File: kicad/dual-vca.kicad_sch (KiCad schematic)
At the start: 57 parts, among them J1 Eurorack Mono Jack, J2 Eurorack Mono Jack, J3 Eurorack Mono Jack, J4 Eurorack Mono Jack, J5 Eurorack Power Small, J6 Eurorack Mono Jack, J7 Eurorack Mono Jack, J8 Conn_02x06_Odd_Even, J9 Conn_02x06_Odd_Even, U1 SSI2164, U2 TL074, U3 LM4040LP-10, U4 LM4040LP-2.5

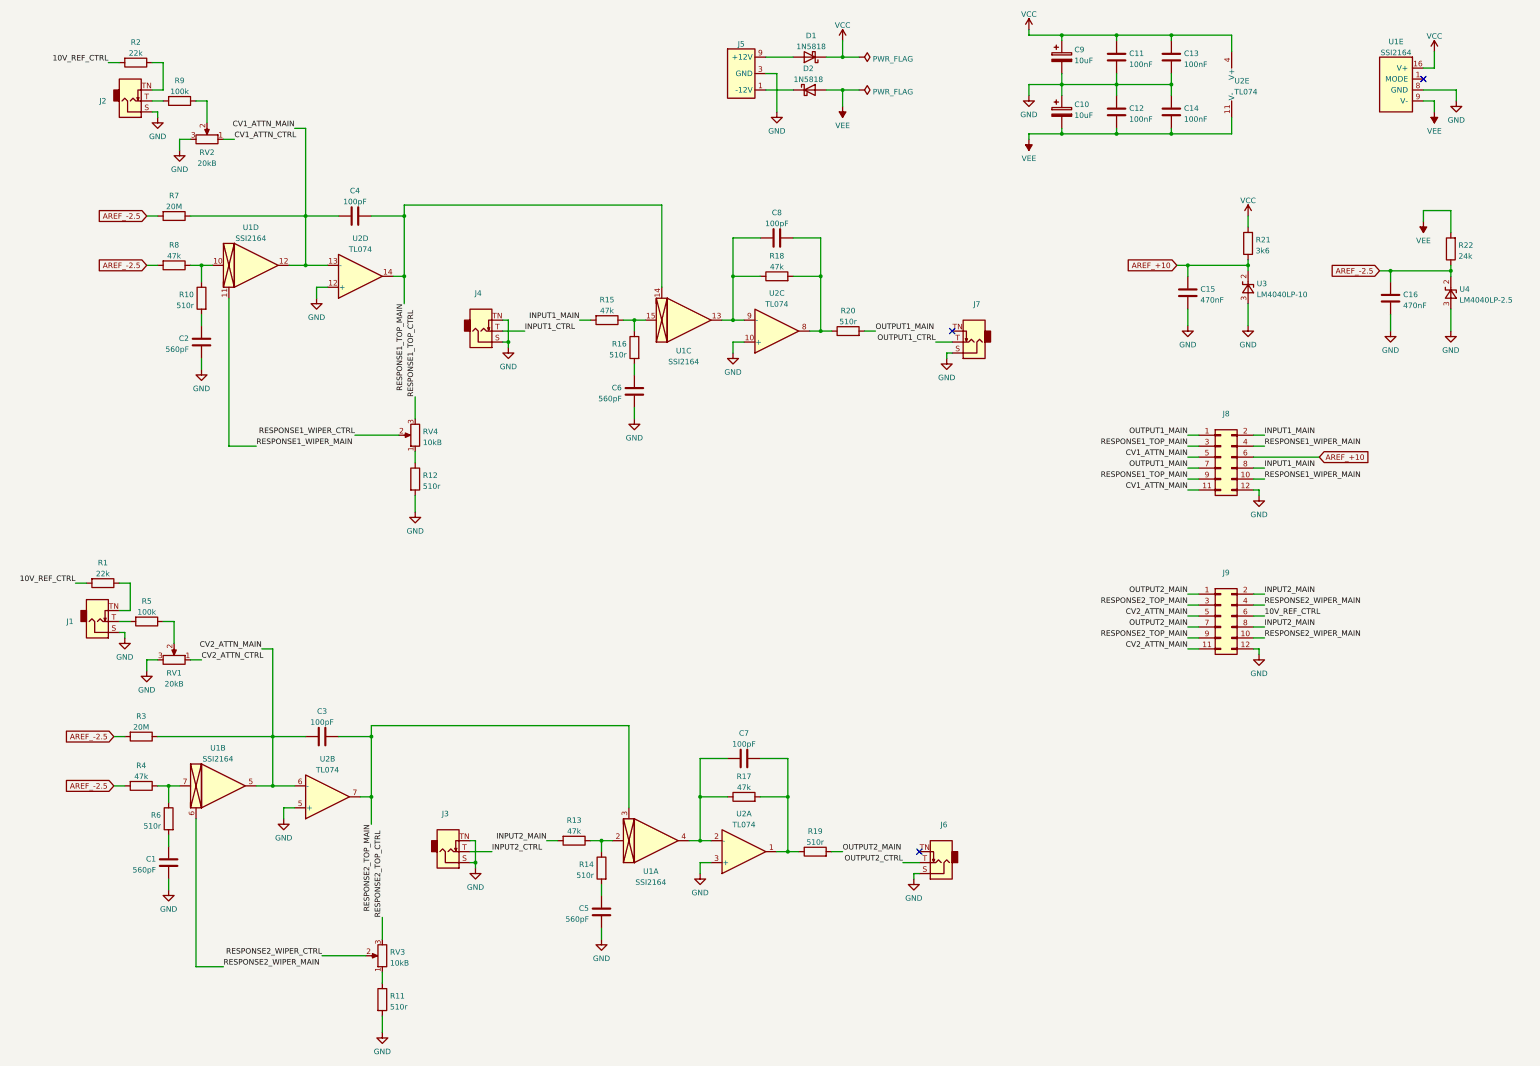
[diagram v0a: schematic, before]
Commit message: Adding beginnings of panel files and routed more of the pcb
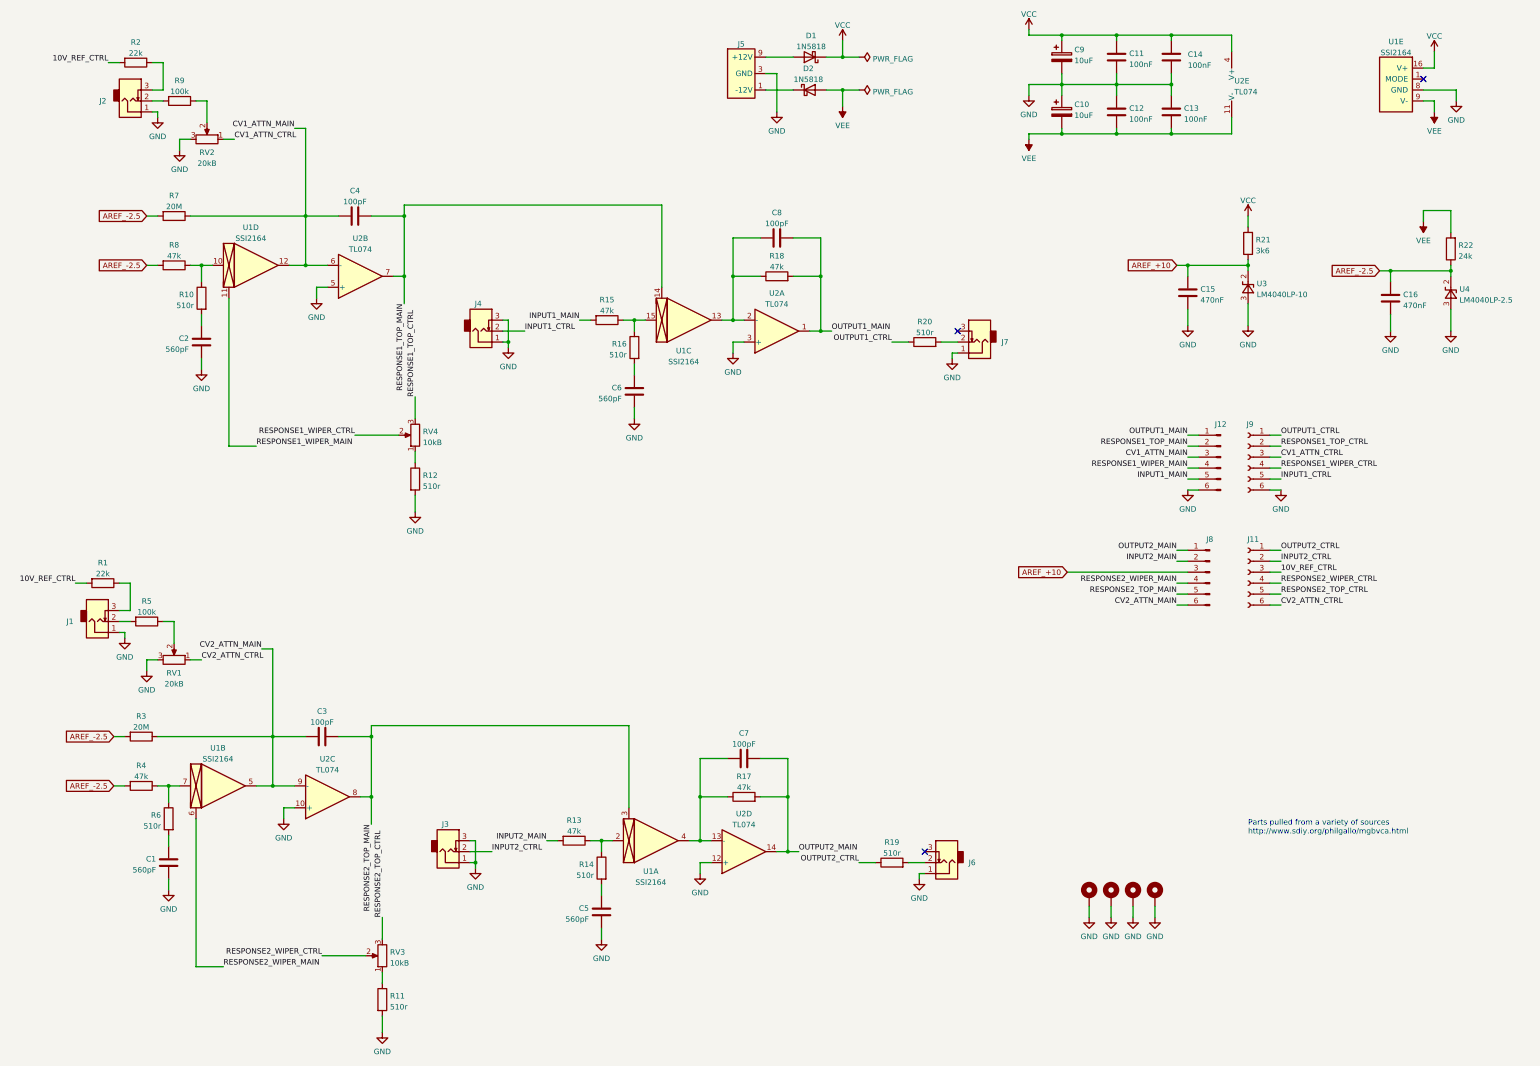
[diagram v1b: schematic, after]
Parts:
- removed J8: Conn_02x06_Odd_Even, Connector_PinHeader_2.54mm:PinHeader_2x06_P2.54mm_Vertical, symbol Connector_Generic:Conn_02x06_Odd_Even
- removed J9: Conn_02x06_Odd_Even, Connector_PinSocket_2.54mm:PinSocket_2x06_P2.54mm_Vertical, symbol Connector_Generic:Conn_02x06_Odd_Even
- added H1, H2, H3, H4: MountingHole_Pad, MountingHole:MountingHole_3.2mm_M3_DIN965_Pad, symbol Mechanical:MountingHole_Pad
- added J11, J9: Conn_01x06_Socket, Connector_PinSocket_2.54mm:PinSocket_1x06_P2.54mm_Vertical, symbol Connector:Conn_01x06_Socket
- added J12, J8: Conn_01x06_Pin, Connector_PinHeader_2.54mm:PinHeader_1x06_P2.54mm_Vertical, symbol Connector:Conn_01x06_Pin
- C1, C11, C12, C13, C14, C15, C16, C2, C3, C4, C5, C6, C7, C8: footprint rumblesan-standard-parts:C_Rect_L7.0mm_W3.5mm_P5.00mm -> Rumblesan_Standard_Parts:C_Rect_L7.0mm_W2.5mm_P5.00mm
- C10, C9: footprint rumblesan-standard-parts:CP_Radial_D5.0mm_P2.00mm -> Rumblesan_Standard_Parts:CP_Radial_D5.0mm_P2.00mm
- D1, D2: footprint rumblesan-standard-parts:D_DO-41_SOD81_P10.16mm_Horizontal -> Rumblesan_Standard_Parts:D_DO-41_SOD81_P10.16mm_Horizontal
- J1, J2, J3, J4, J6, J7: footprint rumblesan-standard-parts:Jack_3.5mm_QingPu_WQP-PJ398SM_Vertical -> Rumblesan_Standard_Parts:Jack_3.5mm_QingPu_WQP-PJ398SM_Vertical; symbol Eurorack_Hardware:Eurorack Mono Jack -> Audio_Connectors:Eurorack_Mono_Jack
- J5: footprint eurorack-power:Eurorack_PowerHeader_2x05_P2.54mm_Shrouded -> Eurorack_Power:Eurorack_PowerHeader_2x05_P2.54mm_Shrouded
- R1, R10, R11, R12, R13, R14, R15, R16, R17, R18, R19, R2, R20, R21, R22, R3, R4, R5, R6, R7, R8, R9: footprint rumblesan-standard-parts:R_Axial_DIN0207_L6.3mm_D2.5mm_P10.16mm_Horizontal -> Rumblesan_Standard_Parts:R_Axial_DIN0207_L6.3mm_D2.5mm_P10.16mm_Horizontal
- RV1, RV2, RV3, RV4: footprint rumblesan-standard-parts:Potentiometer_Alpha_RD901F-40-00D_Single_Vertical -> Rumblesan_Standard_Parts:Potentiometer_Alpha_RD901F-40-00D_Single_Vertical
- U1: footprint rumblesan-standard-parts:DIP-16_W7.62mm_Socket -> Package_DIP:DIP-16_W7.62mm_Socket
- U2: footprint rumblesan-standard-parts:DIP-14_W7.62mm_Socket -> Package_DIP:DIP-14_W7.62mm_Socket
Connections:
- net 10V_REF_CTRL: now also J11.3 (Pin_3)
- net AREF_+10: now also J8.3 (Pin_3)
- net CV1_ATTN_CTRL: now also J9.3 (Pin_3)
- net CV1_ATTN_MAIN: now also U2.6 (-), J12.3 (Pin_3); no longer U2.13 (-)
- net CV2_ATTN_CTRL: now also J11.6 (Pin_6)
- net CV2_ATTN_MAIN: now also U2.9 (-), J8.6 (Pin_6); no longer U2.6 (-)
- net GND: now also C13.1, J1.1 (Sleeve), J2.1 (Sleeve), J3.1 (Sleeve), J3.3 (Tip_normalize), J4.1 (Sleeve), J4.3 (Tip_normalize), J6.1 (Sleeve), J7.1 (Sleeve), H1.1, H2.1, H3.1, H4.1, J12.6 (Pin_6), J9.6 (Pin_6); no longer C13.2, J1.S (Sleeve), J2.S (Sleeve), J3.S (Sleeve), J3.TN (Tip_normalize), J4.S (Sleeve), J4.TN (Tip_normalize), J6.S (Sleeve), J7.S (Sleeve)
- net INPUT1_CTRL: now also J4.2 (Tip), J9.5 (Pin_5); no longer J4.T (Tip)
- net INPUT1_MAIN: now also J12.5 (Pin_5)
- net INPUT2_CTRL: now also J3.2 (Tip), J11.2 (Pin_2); no longer J3.T (Tip)
- net INPUT2_MAIN: now also J8.2 (Pin_2)
- net OUTPUT1_CTRL: now also R20.1, J9.1 (Pin_1); no longer J7.T (Tip)
- net OUTPUT1_MAIN: now also C8.2, R18.2, U2.1, J12.1 (Pin_1); no longer R20.2
- net OUTPUT2_CTRL: now also R19.1, J11.1 (Pin_1); no longer J6.T (Tip)
- net OUTPUT2_MAIN: now also C7.2, R17.2, U2.14, J8.1 (Pin_1); no longer R19.2
- net RESPONSE1_TOP_CTRL: now also J9.2 (Pin_2)
- net RESPONSE1_TOP_MAIN: now also U2.7, J12.2 (Pin_2); no longer U2.14
- net RESPONSE1_WIPER_CTRL: now also J9.4 (Pin_4)
- net RESPONSE1_WIPER_MAIN: now also J12.4 (Pin_4)
- net RESPONSE2_TOP_CTRL: now also J11.5 (Pin_5)
- net RESPONSE2_TOP_MAIN: now also U2.8, J8.5 (Pin_5); no longer U2.7
- net RESPONSE2_WIPER_CTRL: now also J11.4 (Pin_4)
- net RESPONSE2_WIPER_MAIN: now also J8.4 (Pin_4)
- net VCC: now also C14.2; no longer C13.1
- net VEE: now also C13.2; no longer C14.2
- net at C8.1, R18.1, U1.13: now also U2.2 (-); no longer U2.9 (-)
- net at R2.1: now also J2.3 (Tip_normalize); no longer J2.TN (Tip_normalize)
- net at R5.2: now also J1.2 (Tip); no longer J1.T (Tip)
- net at R1.1: now also J1.3 (Tip_normalize); no longer J1.TN (Tip_normalize)
- net at R9.2: now also J2.2 (Tip); no longer J2.T (Tip)
- net at C7.1, R17.1, U1.4: now also U2.13 (-); no longer U2.2 (-)
- new net: J6.2 (Tip), R19.2
- new net: J7.2 (Tip), R20.2
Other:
- note added: "Parts pulled from a variety of sources http://www.sdiy.org/philgallo/mgbvca.html"
- moved on the sheet: C13, C14, J6, J7, R19, R20, U2A, U2B, U2C, U2D

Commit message: Finishing routing PCBs
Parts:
- C1, C11, C12, C13, C14, C15, C16, C2, C3, C4, C5, C6, C7, C8: footprint Rumblesan_Standard_Parts:C_Rect_L7.0mm_W2.5mm_P5.00mm -> Capacitor_THT:C_Rect_L7.0mm_W2.5mm_P5.00mm; symbol rumblesan-standard-parts:C -> Device:C
- C10, C9: footprint Rumblesan_Standard_Parts:CP_Radial_D5.0mm_P2.00mm -> Capacitor_THT:CP_Radial_D5.0mm_P2.00mm; symbol rumblesan-standard-parts:C_Polarized -> Device:C_Polarized
- D1, D2: footprint Rumblesan_Standard_Parts:D_DO-41_SOD81_P10.16mm_Horizontal -> Diode_THT:D_DO-41_SOD81_P10.16mm_Horizontal
- J5: symbol Eurorack_Hardware:Eurorack Power Small -> Eurorack_Power:Eurorack Power Small
- R1, R10, R11, R12, R13, R14, R15, R16, R17, R18, R19, R2, R20, R21, R22, R3, R4, R5, R6, R7, R8, R9: footprint Rumblesan_Standard_Parts:R_Axial_DIN0207_L6.3mm_D2.5mm_P10.16mm_Horizontal -> Resistor_THT:R_Axial_DIN0207_L6.3mm_D2.5mm_P10.16mm_Horizontal; symbol rumblesan-standard-parts:R -> Device:R
- U3, U4: footprint Package_TO_SOT_THT:TO-92_Inline -> Package_TO_SOT_THT:TO-92_Inline_Wide
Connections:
- net 10V_REF_CTRL: now also C15.1, R1.1, R2.1, R21.2, U3.2 (K); no longer J11.3 (Pin_3), R1.2, R2.2
- net AREF_-2.5: now also R22.2, R3.1, R4.1, R7.1, R8.1; no longer R22.1, R3.2, R4.2, R7.2, R8.2
- net CV1_ATTN_CTRL: now also J9.5 (Pin_5); no longer J9.3 (Pin_3)
- net CV1_ATTN_MAIN: now also J12.5 (Pin_5), R7.2; no longer J12.3 (Pin_3), R7.1
- net CV2_ATTN_CTRL: now also J11.5 (Pin_5); no longer J11.6 (Pin_6)
- net CV2_ATTN_MAIN: now also J8.5 (Pin_5), R3.2; no longer J8.6 (Pin_6), R3.1
- net GND: now also J11.3 (Pin_3), J8.3 (Pin_3), R11.1, R12.1; no longer J12.6 (Pin_6), J9.6 (Pin_6), R11.2, R12.2
- net INPUT1_CTRL: now also J9.2 (Pin_2); no longer J9.5 (Pin_5)
- net INPUT1_MAIN: now also J12.2 (Pin_2), R15.1; no longer J12.5 (Pin_5), R15.2
- net INPUT2_MAIN: now also R13.1; no longer R13.2
- net OUTPUT1_CTRL: now also R20.2; no longer R20.1
- net OUTPUT1_MAIN: now also R18.1; no longer R18.2
- net OUTPUT2_CTRL: now also R19.2; no longer R19.1
- net OUTPUT2_MAIN: now also R17.1; no longer R17.2
- net RESPONSE1_TOP_CTRL: now also J9.4 (Pin_4); no longer J9.2 (Pin_2)
- net RESPONSE1_TOP_MAIN: now also J12.4 (Pin_4); no longer J12.2 (Pin_2)
- net RESPONSE1_WIPER_CTRL: now also J9.6 (Pin_6); no longer J9.4 (Pin_4)
- net RESPONSE1_WIPER_MAIN: now also J12.6 (Pin_6); no longer J12.4 (Pin_4)
- net RESPONSE2_TOP_CTRL: now also J11.4 (Pin_4); no longer J11.5 (Pin_5)
- net RESPONSE2_TOP_MAIN: now also J8.4 (Pin_4); no longer J8.5 (Pin_5)
- net RESPONSE2_WIPER_CTRL: now also J11.6 (Pin_6); no longer J11.4 (Pin_4)
- net RESPONSE2_WIPER_MAIN: now also J8.6 (Pin_6); no longer J8.4 (Pin_4)
- net VCC: now also J12.3 (Pin_3); no longer R21.2
- net VEE: now also R22.1; no longer R22.2
- net at C8.1, U1.13, U2.2 (-): now also R18.2; no longer R18.1
- net at RV4.1: now also R12.2; no longer R12.1
- net at J2.3 (Tip_normalize): now also R2.2; no longer R2.1
- net at RV3.1: now also R11.2; no longer R11.1
- net at C7.1, U1.4, U2.13 (-): now also R17.2; no longer R17.1
- net at J6.2 (Tip): now also R19.1; no longer R19.2
- net at J1.2 (Tip): now also R5.1; no longer R5.2
- net at J1.3 (Tip_normalize): now also R1.2; no longer R1.1
- net at RV1.2: now also R5.2; no longer R5.1
- net at C5.2: now also R14.1; no longer R14.2
- net at R16.2: now also R15.2, U1.15; no longer C6.2
- net at C1.2: now also R6.1; no longer R6.2
- net at R9.1: now also J2.2 (Tip); no longer RV2.2
- net at R9.2: now also RV2.2; no longer J2.2 (Tip)
- net at R10.2: now also R8.2, U1.10; no longer C2.2
- net at J7.2 (Tip): now also R20.1; no longer R20.2
- removed net AREF_+10: C15.1, J8.3 (Pin_3), R21.1, U3.2 (K)
- new net: C6.2, R16.1
- new net: R4.2, R6.2, U1.7
- new net: R13.2, R14.2, U1.2
- new net: C2.2, R10.1
- new net VCC_CTRL: J9.3 (Pin_3), R21.1

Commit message: Fixes for revision 2
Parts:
- added R23: 6k8, Resistor_THT:R_Axial_DIN0207_L6.3mm_D2.5mm_P10.16mm_Horizontal, symbol Device:R
- H1, H2, H3, H4: now left out of the parts list
- J1, J2, J3, J4, J6, J7: footprint Rumblesan_Standard_Parts:Jack_3.5mm_QingPu_WQP-PJ398SM_Vertical -> Rumblesan_Audio_Connectors:Jack_3.5mm_QingPu_WQP-PJ398SM_Vertical; symbol Audio_Connectors:Eurorack_Mono_Jack -> Connector_Audio:AudioJack2_SwitchT
- J5: footprint Eurorack_Power:Eurorack_PowerHeader_2x05_P2.54mm_Shrouded -> Rumblesan_Eurorack_Power:Eurorack_PowerHeader_2x05_P2.54mm_Shrouded; symbol Eurorack_Power:Eurorack Power Small -> Rumblesan_Eurorack_Power:Eurorack Power Small
- R21: value 3k6 -> 1k
- R22: value 24k -> 47k
- RV1, RV2, RV3, RV4: footprint Rumblesan_Standard_Parts:Potentiometer_Alpha_RD901F-40-00D_Single_Vertical -> Rumblesan_Potentiometer_THT:Potentiometer_Alpha_RD901F-40-00D_Single_Vertical
- U1: symbol Audio_Chips:SSI2164 -> Rumblesan_Audio_Chips:SSI2164
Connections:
- net AREF_-2.5: now also U4.3 (A); no longer U4.2 (K)
- net CV1_ATTN_CTRL: now also RV2.3; no longer RV2.1
- net CV2_ATTN_CTRL: now also RV1.3; no longer RV1.1
- net GND: now also J1.S, J2.S, J3.S, J3.TN, J4.S, J4.TN, J6.TN, J7.S, RV1.1, RV2.1, U4.2 (K); no longer J1.1 (Sleeve), J2.1 (Sleeve), J3.1 (Sleeve), J3.3 (Tip_normalize), J4.1 (Sleeve), J4.3 (Tip_normalize), J6.1 (Sleeve), J7.1 (Sleeve), RV1.3, RV2.3, U4.3 (A)
- net INPUT1_CTRL: now also J4.T; no longer J4.2 (Tip)
- net INPUT2_CTRL: now also J3.T; no longer J3.2 (Tip)
- net VCC: now also R23.2
- net at R2.2: now also J2.TN; no longer J2.3 (Tip_normalize)
- net at R19.1: now also J6.T; no longer J6.2 (Tip)
- net at R5.1: now also J1.T; no longer J1.2 (Tip)
- net at R1.2: now also J1.TN; no longer J1.3 (Tip_normalize)
- net at U1.1 (MODE): now also R23.1
- net at R9.1: now also J2.T; no longer J2.2 (Tip)
- net at R20.1: now also J7.T; no longer J7.2 (Tip)
- no-connect marks 3 -> 2
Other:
- note added: "0.2mA delivered 0.1mA needed"
- note added: "1.5mA delivered 0.75mA needed"
- note added: "Parts pulled from a variety of sources http://www.sdiy.org/philgallo/mgbvca.html https://pichenettes.github.io/mutable-instruments-documentation/modules/veils_2020/"
- note removed: "Parts pulled from a variety of sources http://www.sdiy.org/philgallo/mgbvca.html"
- company: (none) -> Bristol Communal Modular
- title: (none) -> Dual VCA
- moved on the sheet: J6, J7, RV1, RV2, U4

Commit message: Minor tweaks and tidying
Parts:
- C11, C12, C13, C14: Spec ceramic C0G -> ceramic X7R
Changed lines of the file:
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@@
 		(title "Dual VCA")
 		(date "2024-07-04")
-		(rev "02")
+		(rev "rev02")
 		(company "Bristol Communal Modular")
 		(comment 2 "creativecommons.org/licenses/by/4.0/")
@@
 			)
 		)
-		(property "Spec" "ceramic C0G"
+		(property "Spec" "ceramic X7R"
 			(at 306.07 46.99 90)
 			(effects
@@
 			)
 		)
-		(property "Spec" "ceramic C0G"
+		(property "Spec" "ceramic X7R"
 			(at 311.15 34.29 90)
 			(effects
@@
 			)
 		)
-		(property "Spec" "ceramic C0G"
+		(property "Spec" "ceramic X7R"
 			(at 318.77 46.99 90)
 			(effects
@@
 			)
 		)
-		(property "Spec" "ceramic C0G"
+		(property "Spec" "ceramic X7R"
 			(at 306.07 34.29 90)
 			(effects
